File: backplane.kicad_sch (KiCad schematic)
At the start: 2 parts, among them J1 DIN-41612-connector_090319679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

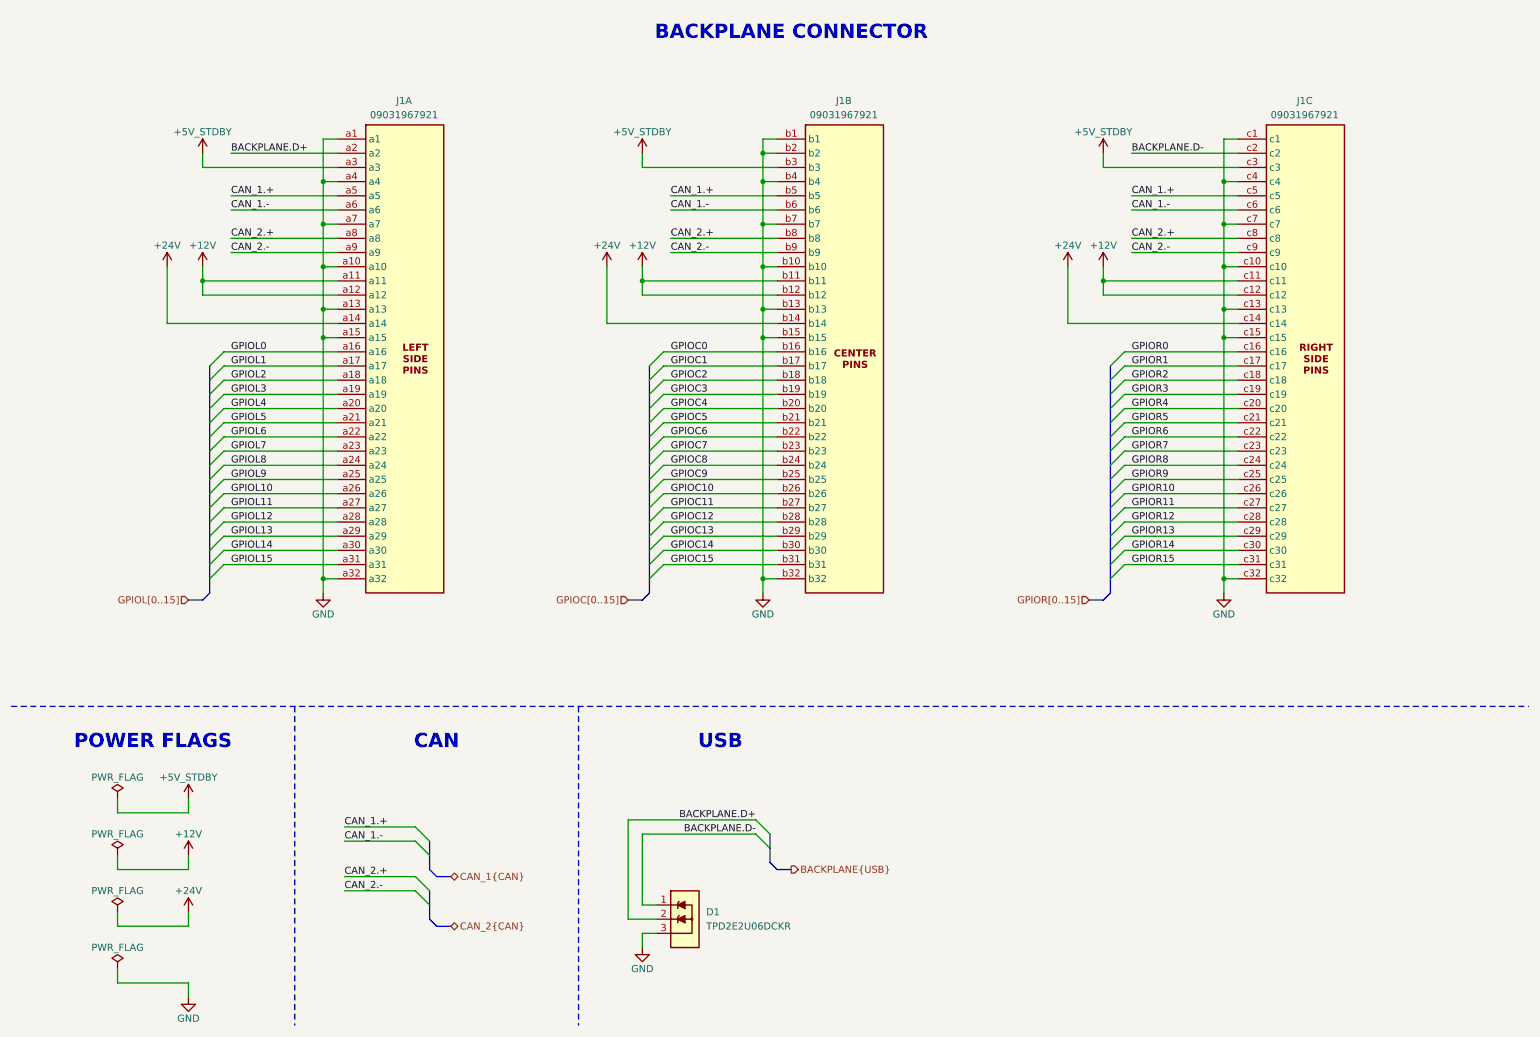
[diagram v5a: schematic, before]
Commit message: [#1] WIP: Refactor schematic
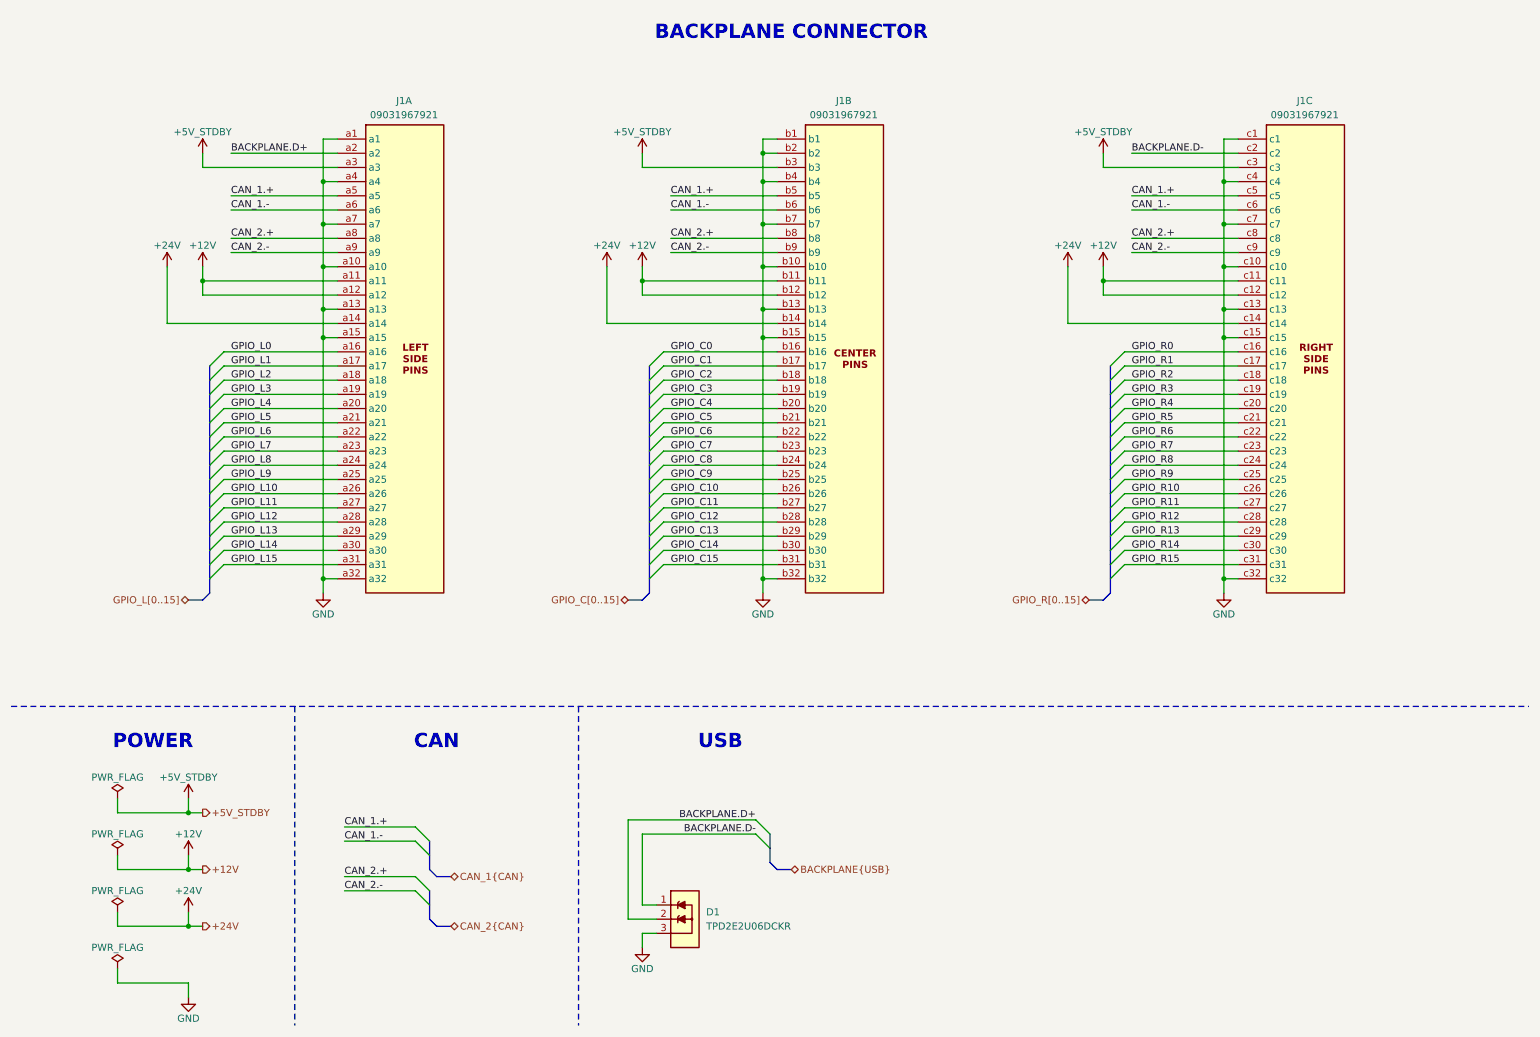
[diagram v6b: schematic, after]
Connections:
- net GPIOC0 renamed GPIO_C0
- net GPIOC1 renamed GPIO_C1
- net GPIOC10 renamed GPIO_C10
- net GPIOC11 renamed GPIO_C11
- net GPIOC12 renamed GPIO_C12
- net GPIOC13 renamed GPIO_C13
- net GPIOC14 renamed GPIO_C14
- net GPIOC15 renamed GPIO_C15
- net GPIOC2 renamed GPIO_C2
- net GPIOC3 renamed GPIO_C3
- net GPIOC4 renamed GPIO_C4
- net GPIOC5 renamed GPIO_C5
- net GPIOC6 renamed GPIO_C6
- net GPIOC7 renamed GPIO_C7
- net GPIOC8 renamed GPIO_C8
- net GPIOC9 renamed GPIO_C9
- net GPIOL0 renamed GPIO_L0
- net GPIOL1 renamed GPIO_L1
- net GPIOL10 renamed GPIO_L10
- net GPIOL11 renamed GPIO_L11
- net GPIOL12 renamed GPIO_L12
- net GPIOL13 renamed GPIO_L13
- net GPIOL14 renamed GPIO_L14
- net GPIOL15 renamed GPIO_L15
- net GPIOL2 renamed GPIO_L2
- net GPIOL3 renamed GPIO_L3
- net GPIOL4 renamed GPIO_L4
- net GPIOL5 renamed GPIO_L5
- net GPIOL6 renamed GPIO_L6
- net GPIOL7 renamed GPIO_L7
- net GPIOL8 renamed GPIO_L8
- net GPIOL9 renamed GPIO_L9
- net GPIOR0 renamed GPIO_R0
- net GPIOR1 renamed GPIO_R1
- net GPIOR10 renamed GPIO_R10
- net GPIOR11 renamed GPIO_R11
- net GPIOR12 renamed GPIO_R12
- net GPIOR13 renamed GPIO_R13
- net GPIOR14 renamed GPIO_R14
- net GPIOR15 renamed GPIO_R15
- net GPIOR2 renamed GPIO_R2
- net GPIOR3 renamed GPIO_R3
- net GPIOR4 renamed GPIO_R4
- net GPIOR5 renamed GPIO_R5
- net GPIOR6 renamed GPIO_R6
- net GPIOR7 renamed GPIO_R7
- net GPIOR8 renamed GPIO_R8
- net GPIOR9 renamed GPIO_R9
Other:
- note added: "POWER"
- note removed: "POWER FLAGS"

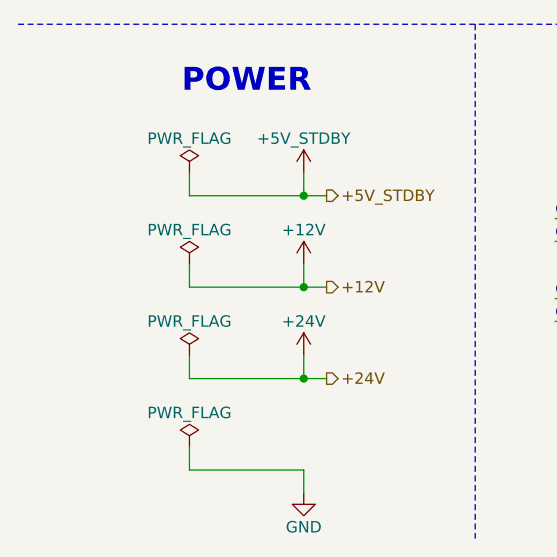
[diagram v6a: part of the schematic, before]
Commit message: [#1] WIP: Refactor schematic
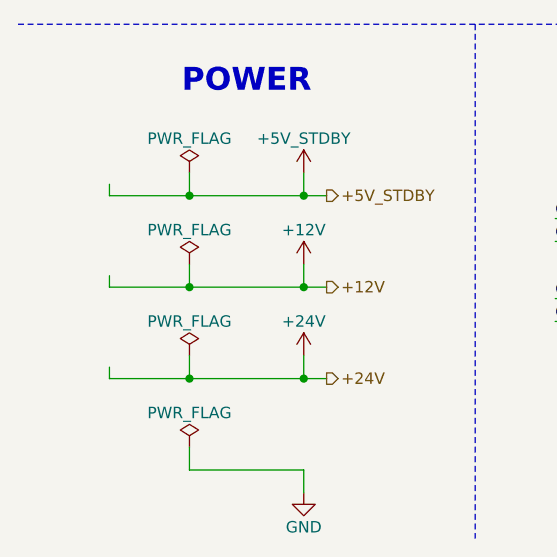
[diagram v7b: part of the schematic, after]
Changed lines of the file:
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@@
 	)
 	(junction
+		(at 31.75 158.75)
+		(diameter 0)
+		(color 0 0 0 0)
+	)
+	(junction
 		(at 44.45 158.75)
 		(diameter 0)
@@
 	)
 	(junction
+		(at 31.75 179.07)
+		(diameter 0)
+		(color 0 0 0 0)
+	)
+	(junction
 		(at 229.87 60.96)
 		(diameter 0)
@@
 	)
 	(junction
+		(at 31.75 168.91)
+		(diameter 0)
+		(color 0 0 0 0)
+	)
+	(junction
 		(at 229.87 45.72)
 		(diameter 0)
@@
 	(wire
 		(pts
+			(xy 22.86 157.48) (xy 22.86 158.75)
+		)
+		(stroke
+			(width 0)
+			(type default)
+		)
+	)
+	(wire
+		(pts
 			(xy 50.8 81.28) (xy 71.12 81.28)
 		)
@@
 		)
 	)
+	(wire
+		(pts
+			(xy 22.86 168.91) (xy 31.75 168.91)
+		)
+		(stroke
+			(width 0)
+			(type default)
+		)
+	)
 	(bus
 		(pts
@@
 	(wire
 		(pts
+			(xy 22.86 158.75) (xy 31.75 158.75)
+		)
+		(stroke
+			(width 0)
+			(type default)
+		)
+	)
+	(wire
+		(pts
 			(xy 71.12 38.1) (xy 68.58 38.1)
 		)
@@
 	(wire
 		(pts
+			(xy 22.86 167.64) (xy 22.86 168.91)
+		)
+		(stroke
+			(width 0)
+			(type default)
+		)
+	)
+	(wire
+		(pts
 			(xy 44.45 176.53) (xy 44.45 179.07)
 		)
@@
 	(wire
 		(pts
+			(xy 22.86 179.07) (xy 31.75 179.07)
+		)
+		(stroke
+			(width 0)
+			(type default)
+		)
+	)
+	(wire
+		(pts
 			(xy 71.12 55.88) (xy 52.07 55.88)
 		)
@@
 	(wire
 		(pts
+			(xy 22.86 177.8) (xy 22.86 179.07)
+		)
+		(stroke
+			(width 0)
+			(type default)
+		)
+	)
+	(wire
+		(pts
 			(xy 129.54 76.2) (xy 149.86 76.2)
 		)
@@
 		(length 2.54)
 		(shape round)
+		(at 22.86 177.8 0)
+		(effects
+			(font
+				(size 1.27 1.27)
+			)
+			(justify left bottom)
+		)
+		(property "Netclass" "PWR"
+			(at 22.86 172.974 0)
+			(effects
+				(font
+					(size 1.27 1.27)
+				)
+			)
+		)
+		(property "Component Class" ""
+			(at -228.6 7.62 0)
+			(effects
+				(font
+					(size 1.27 1.27)
+					(italic yes)
+				)
+			)
+		)
+	)
+	(netclass_flag ""
+		(length 2.54)
+		(shape round)
 		(at 171.45 156.21 0)
 		(effects
@@
 			(effects
 				(font
+					(size 1.27 1.27)
+					(italic yes)
+				)
+			)
+		)
+	)
+	(netclass_flag ""
+		(length 2.54)
+		(shape round)
+		(at 22.86 167.64 0)
+		(effects
+			(font
+				(size 1.27 1.27)
+			)
+			(justify left bottom)
+		)
+		(property "Netclass" "PWR"
+			(at 22.86 162.814 0)
+			(effects
+				(font
+					(size 1.27 1.27)
+				)
+			)
+		)
+		(property "Component Class" ""
+			(at -228.6 -2.54 0)
+			(effects
+				(font
+					(size 1.27 1.27)
+					(italic yes)
+				)
+			)
+		)
+	)
+	(netclass_flag ""
+		(length 2.54)
+		(shape round)
+		(at 22.86 157.48 0)
+		(effects
+			(font
+				(size 1.27 1.27)
+			)
+			(justify left bottom)
+		)
+		(property "Netclass" "PWR"
+			(at 22.86 152.654 0)
+			(effects
+				(font
+					(size 1.27 1.27)
+				)
+			)
+		)
+		(property "Component Class" ""
+			(at -228.6 -12.7 0)
+			(effects
+				(font

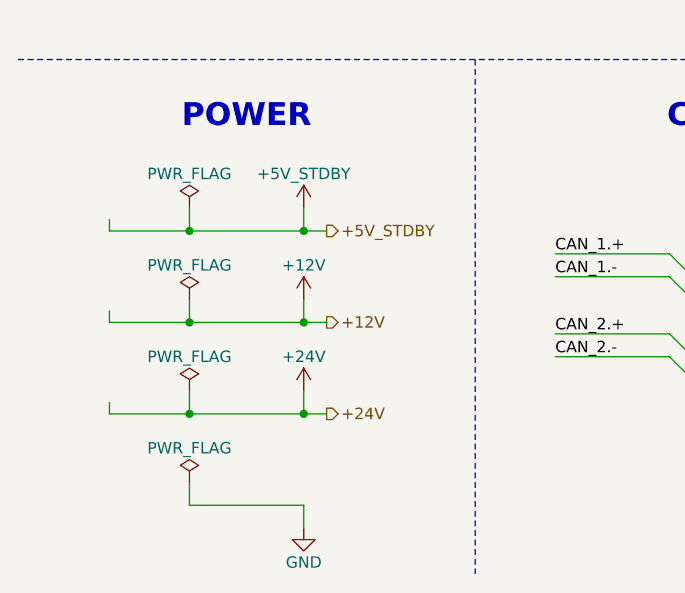
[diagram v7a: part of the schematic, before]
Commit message: [#3] Add CM5 RTC battery
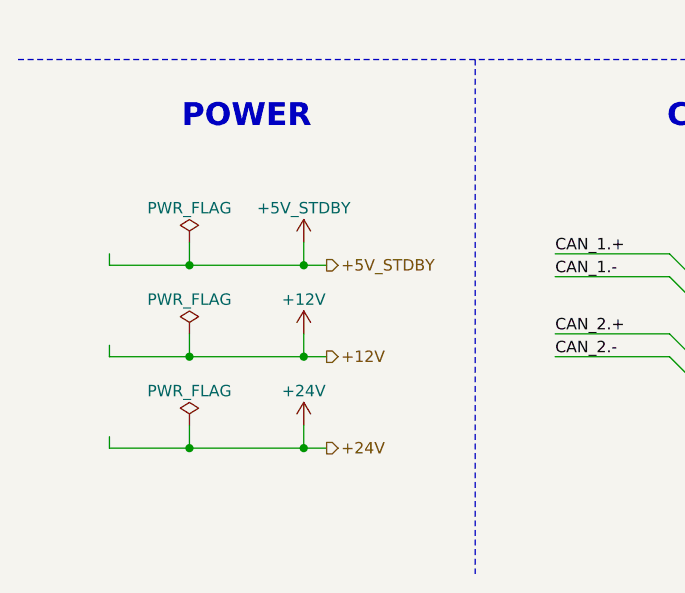
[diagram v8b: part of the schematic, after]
